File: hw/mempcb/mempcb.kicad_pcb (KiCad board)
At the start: 2 copper layers, 100 x 100 mm, 32 parts, among them J1 RC6502_Bus, J2 0.1" 2x25, U3 JEDEC_DIP32_RAM, U4 74LS138, U5 74LS138

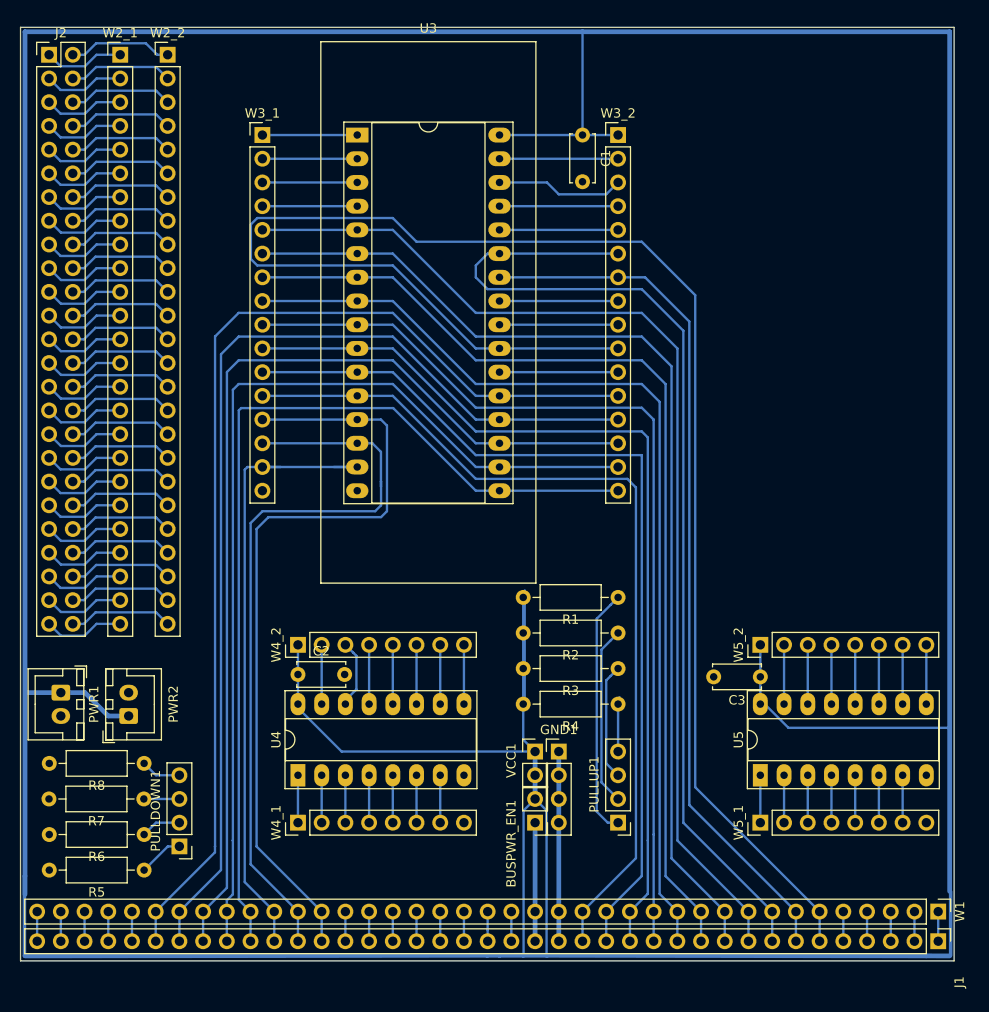
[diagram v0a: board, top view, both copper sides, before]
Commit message: hw/mempcb: Widen board edge to 0.4 mm; tweak corners
According to [1], fabs cut along the _center_ of the board edge line, so
you can make it as wide as you want. Thus a cheap and easy way of ensuring
you maintain margin at the edge of the board is to widen the board line to
twice the margin you need, because KiCad will not let traces etc. _enter_
the line.

I can't check this on 5.0 because the DRC doesn't check for traces
exceeding the board boundary, but I believe that 5.1 does check for this,
so we can test it there.

[1]: https://forum.kicad.info/t/margin-or-edge-cuts/10341/2
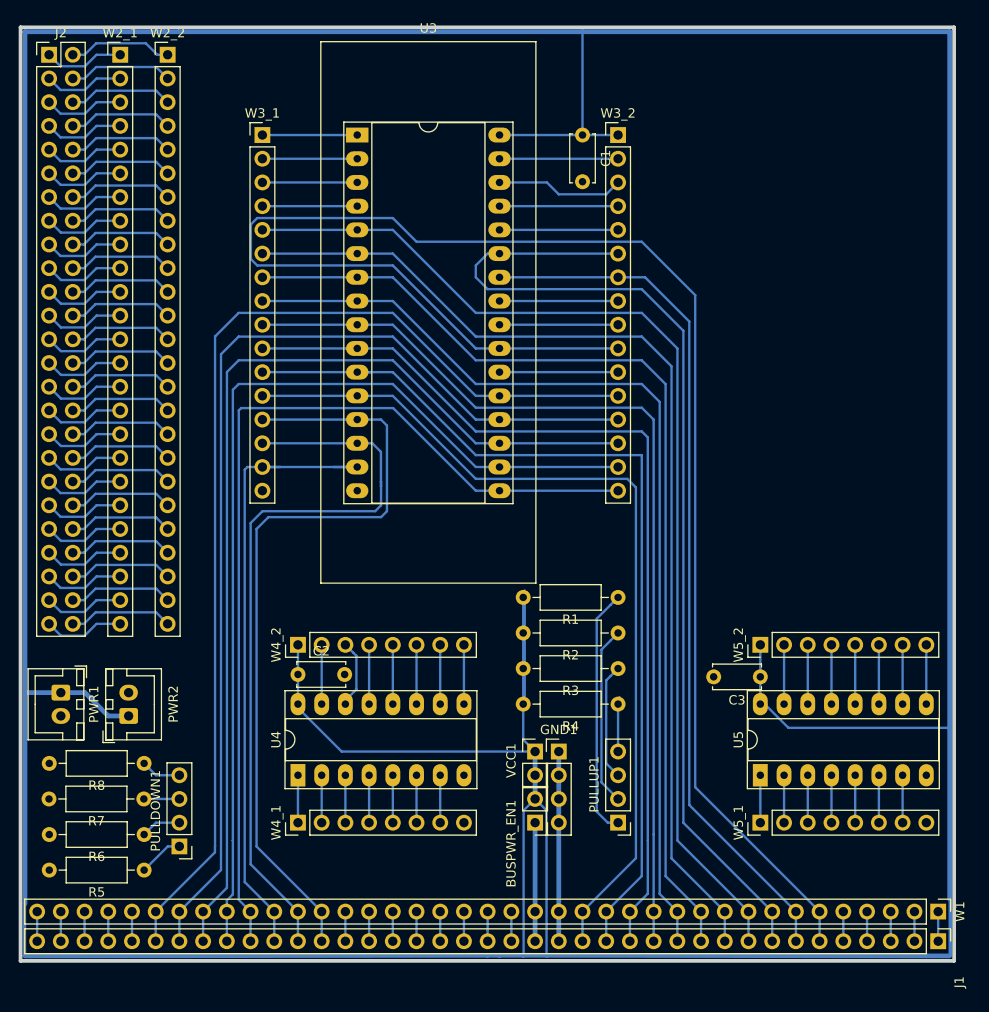
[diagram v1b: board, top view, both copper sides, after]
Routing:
- net /VCC: track 565.0 -> 563.8 mm
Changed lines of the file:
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@@
     (thickness 1.6002)
     (drawings 4)
-    (tracks 525)
+    (tracks 524)
     (zones 0)
     (modules 32)
@@
     )
   )
-  (gr_line (start 101.702 152.102) (end 101.702 52.102) (layer Edge.Cuts) (width 0.0381))
-  (gr_line (start 201.702 152.102) (end 101.702 152.102) (layer Edge.Cuts) (width 0.0381))
-  (gr_line (start 201.702 152.102) (end 201.702 52.102) (layer Edge.Cuts) (width 0.0381))
-  (gr_line (start 101.702 52.102) (end 201.702 52.102) (layer Edge.Cuts) (width 0.0381))
+  (gr_line (start 101.702 152.102) (end 101.702 52.102) (layer Edge.Cuts) (width 0.4))
+  (gr_line (start 201.702 152.102) (end 101.702 152.102) (layer Edge.Cuts) (width 0.4))
+  (gr_line (start 201.702 152.102) (end 201.702 52.102) (layer Edge.Cuts) (width 0.4))
+  (gr_line (start 101.702 52.102) (end 201.702 52.102) (layer Edge.Cuts) (width 0.4))
   (segment (start 153.01 63.64) (end 165.71 63.64) (width 0.254) (layer Back) (net 1) (status 30))
   (segment (start 152.61 63.64) (end 153.01 63.64) (width 0.254) (layer Front) (net 1) (status 30))
@@
   (segment (start 153.01 151.50535) (end 155.56 151.50194) (width 0.508) (layer Back) (net 1))
   (segment (start 201.27 144.693) (end 201.228 144.651) (width 0.254) (layer Back) (net 1))
-  (segment (start 201.334 151.5296) (end 201.334 144.693) (width 0.381) (layer Back) (net 1))
+  (segment (start 201.295 151.5296) (end 201.295 144.693) (width 0.371) (layer Back) (net 1))
   (segment (start 201.228 151.5716) (end 201.27 151.5296) (width 0.254) (layer Back) (net 1))
   (segment (start 198.73 151.567789) (end 201.228 151.5716) (width 0.508) (layer Back) (net 1))
-  (segment (start 102.176 143.015) (end 102.176 145) (width 0.508) (layer Back) (net 1))
-  (segment (start 102.116 151.5716) (end 102.116 143.015) (width 0.381) (layer Back) (net 1))
-  (segment (start 102.176 52.576) (end 102.176 143.015) (width 0.508) (layer Back) (net 1))
+  (segment (start 102.116 151.5716) (end 102.116 146) (width 0.381) (layer Back) (net 1))
+  (segment (start 102.176 52.576) (end 102.176 146) (width 0.508) (layer Back) (net 1))
   (segment (start 161.9 63.64) (end 161.9 52.576) (width 0.254) (layer Back) (net 1))
   (segment (start 161.9 52.576) (end 102.176 52.576) (width 0.508) (layer Back) (net 1))
@@
   (segment (start 201.228 127.14) (end 201.228 52.576) (width 0.508) (layer Back) (net 1))
   (segment (start 183.9598 127.14) (end 201.228 127.14) (width 0.254) (layer Back) (net 1))
-  (segment (start 201.228 144.651) (end 201.228 127.14) (width 0.508) (layer Back) (net 1))
+  (segment (start 201.228 145.5) (end 201.228 127.14) (width 0.508) (layer Back) (net 1))
   (segment (start 131.42 124.6) (end 131.42 118.25) (width 0.254) (layer Back) (net 1))
   (segment (start 151.706 151.50535) (end 153.01 151.50535) (width 0.508) (layer Back) (net 1))

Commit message: hw/mempcb: Clean up board edges and fix clearances
- Move RC6502 bus wire-wrap connector down to be flush against the bus
  bus pins. (The 90 degree connector has a low profile so won't get
  in the way of wire wrap.)
- KiCad 5.1 DRC now checks board edge clearance to center of the edge
  cut line, so we need not check this manually. Thus we can bring board
  edge cut line width back to default 0.0381 to avoid potential problems
  with the fab, and also to have less blocking against edge of cut
  line when routing.
- Redraw the 20 mil outside edge Vcc line now to conform with the default
  0.254 mm clearance (to board edge, in this case).
- Rework the narrower connections on board edge Vcc around the RC6502 bus
  connector to have maximum width possible between the pins and the edge.

TODO:
- Clean up traces at RC6502 bus wire-wrap connector.
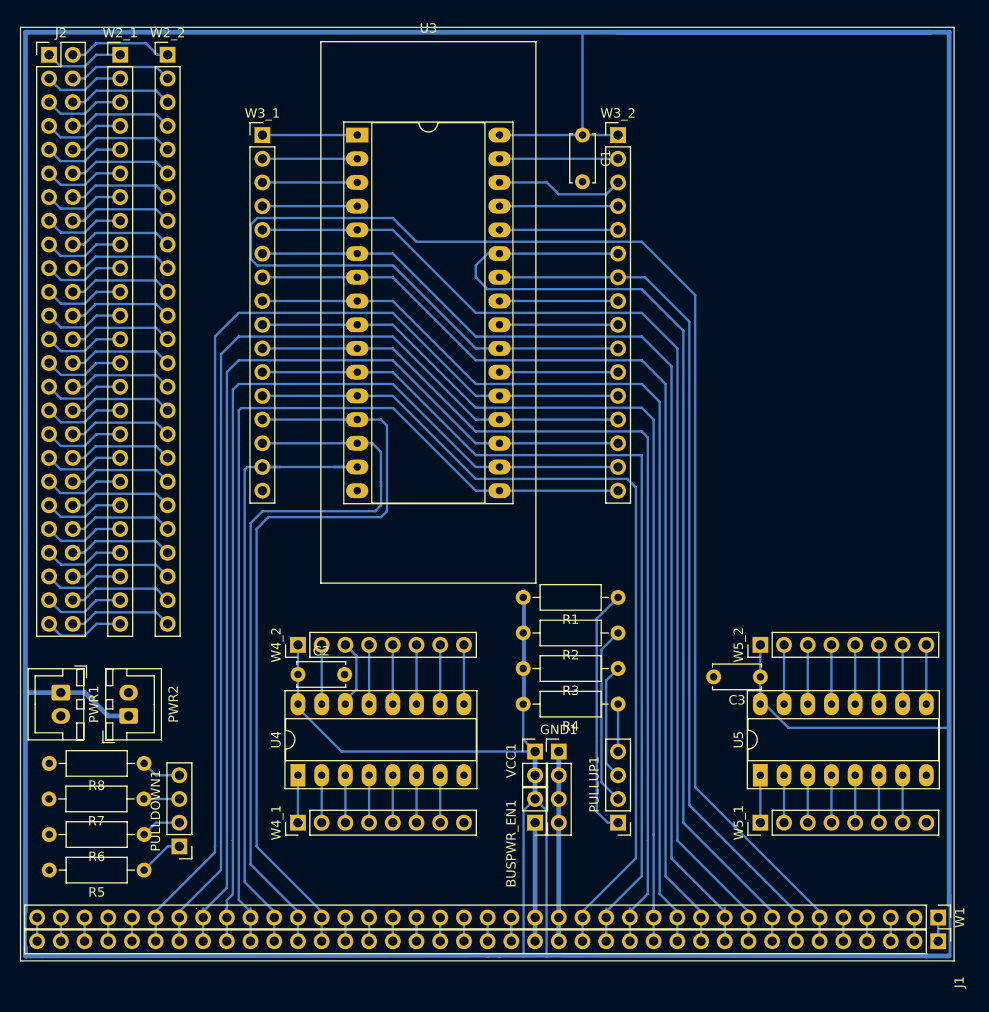
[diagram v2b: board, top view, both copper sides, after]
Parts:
- moved W1 0.64 mm to (200.0, 147.5)
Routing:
- net /VCC: track 563.8 -> 608.6 mm

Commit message: hw/mempcb: Rename most references and remove some from silkscreen
We rename the ICs to U1, U2 and U3 so that it doesn't look like some are
missing. We resolve the previous collisions with the wire-wrap headers by
renaming them all to WW_*.1 and WW_*.2 where * is the part with which
they're associated. The reference alignment and locations are also cleaned
up a bit.

Update the PCB from this, make invisible the skilk screen references for
the WW_* headers (since their associated part is easily clear from
proximity) and for the others move the silk screen to locations that are
more clear.
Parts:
- removed W3_1: 0.1" 1x16, Connector_PinHeader_2.54mm:PinHeader_1x16_P2.54mm_Vertical
- added WW_U1.1: 0.1" 1x16, Connector_PinHeader_2.54mm:PinHeader_1x16_P2.54mm_Vertical, F.Cu at (127.6, 63.6)
- renumbered U3 to U1, U4 to U2, U5 to U3, W1 to WW_J1, W2_1 to WW_J2.1, W2_2 to WW_J2.2, W3_2 to WW_U1.2, W4_1 to WW_U2.1, W4_2 to WW_U2.2, W5_1 to WW_U3.1, W5_2 to WW_U3.2

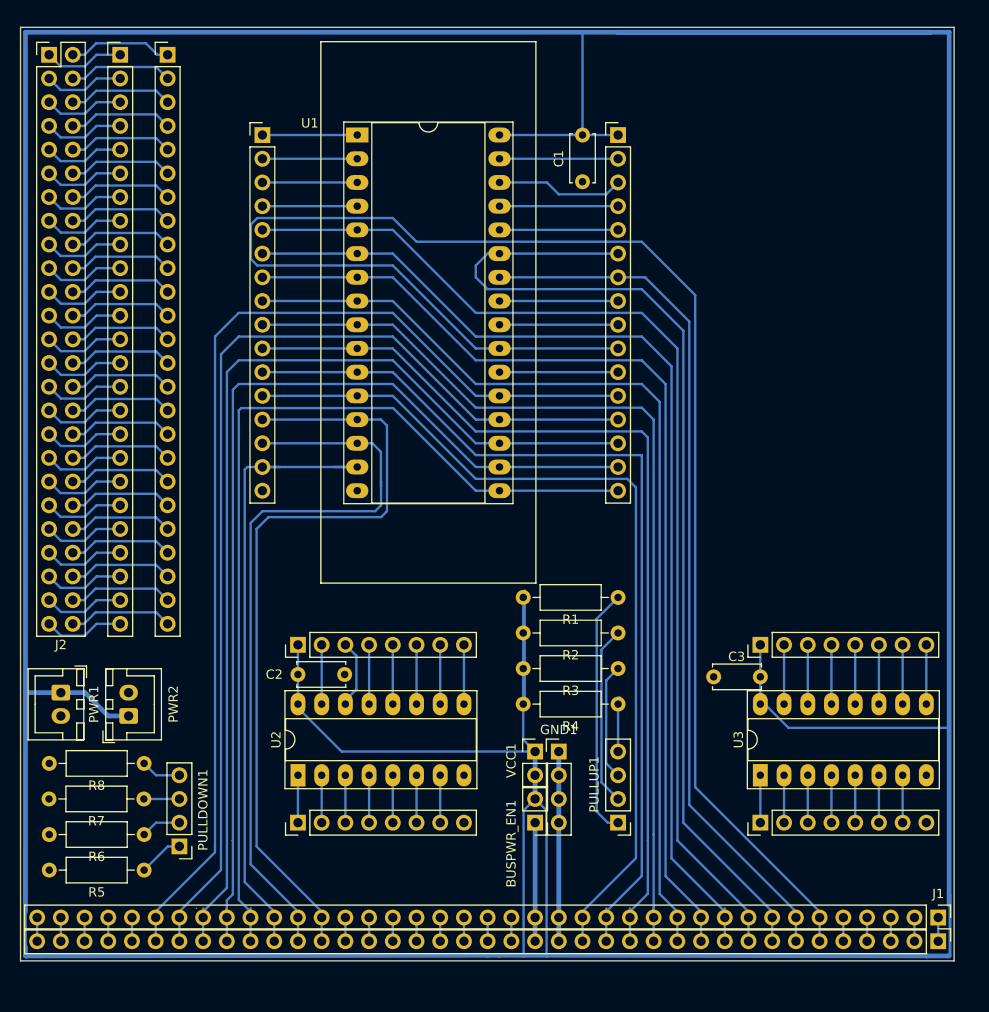
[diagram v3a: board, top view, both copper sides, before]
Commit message: hw/mempcb: Rename, rework and swap position of pull-ups/downs
- Rename PULLDOWN1 to PULLDOWN2
- Rename associated resistors to R1.1, R1.2 etc. for PULLUP1, and R2.1,
  R2.2 for PULLDOWN2.
- Make the resistor silks smaller, rotated and across the middle, so that
  they're out of the way but readable under the resistor, now now one can
  see which pins on the header they match. Nonetheless, also add pin
  numbers to the PULLDOWN2 header, since it's not lined up with the
  resistors like PULLUP1 is.
- Swap the pull-ups and pull-downs: having the pull-ups next to the power
  connectors is a bit more intuitive, and also makes for easier power
  distribution.

Also remove a couple of unconnected traces on the RC6502 header.
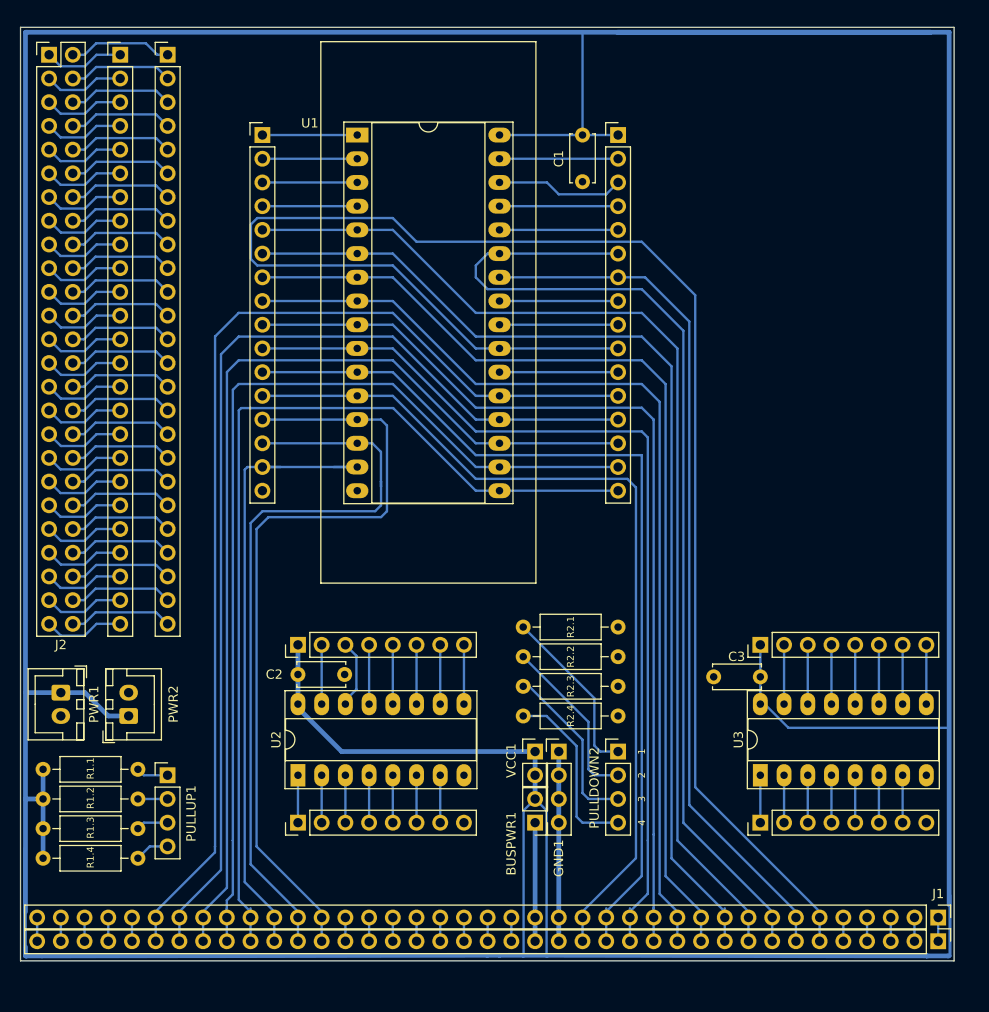
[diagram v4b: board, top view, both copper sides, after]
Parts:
- removed PULLDOWN1: 0.1" 1x4, Connector_PinHeader_2.54mm:PinHeader_1x04_P2.54mm_Vertical
- added PULLDOWN2: 0.1" 1x4, Connector_PinHeader_2.54mm:PinHeader_1x04_P2.54mm_Vertical, F.Cu at (165.7, 129.7)
- moved R1.1 54.6 mm to (114.3, 131.6)
- moved R1.2 54.4 mm to (114.3, 134.8)
- moved R1.3 54.2 mm to (114.3, 137.9)
- moved R1.4 54.0 mm to (114.3, 141.1)
- moved PULLUP1 48.5 mm to (117.5, 132.2), turned to 0 degrees
- moved R2.1 48.2 mm to (155.6, 116.3), turned to 0 degrees
- moved R2.2 44.9 mm to (155.6, 119.5), turned to 0 degrees
- moved R2.3 42.4 mm to (155.6, 122.7), turned to 0 degrees
- moved R2.4 40.9 mm to (155.6, 125.9), turned to 0 degrees
- renumbered BUSPWR_EN1 to BUSPWR1, R1 to R1.1, R2 to R1.2, R3 to R1.3, R4 to R1.4, R5 to R2.1, R6 to R2.2, R7 to R2.3, R8 to R2.4
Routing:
- net Net-(PULLUP1-Pad1): track 26.7 -> 4.34 mm
- net /VCC: track 608.6 -> 591.5 mm
- net Net-(PULLUP1-Pad2): track 19.3 -> 3.17 mm
- net Net-(PULLDOWN2-Pad4): track 4.31 -> 19.3 mm
- net Net-(PULLDOWN2-Pad3): track 3.81 -> 18.5 mm
- net Net-(PULLDOWN2-Pad2): track 4.31 -> 18.4 mm
- net Net-(PULLDOWN2-Pad1): track 4.83 -> 18.7 mm
- net Net-(PULLUP1-Pad3): track 12.5 -> 3.44 mm
- net Net-(PULLUP1-Pad4): track 5.29 -> 3.70 mm

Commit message: hw/mempcb: Clean up addr/data lines at RC6502 header
This fixes the weird pad entries that were left after moving
the wire-wrap header down to butt against the bus connector.
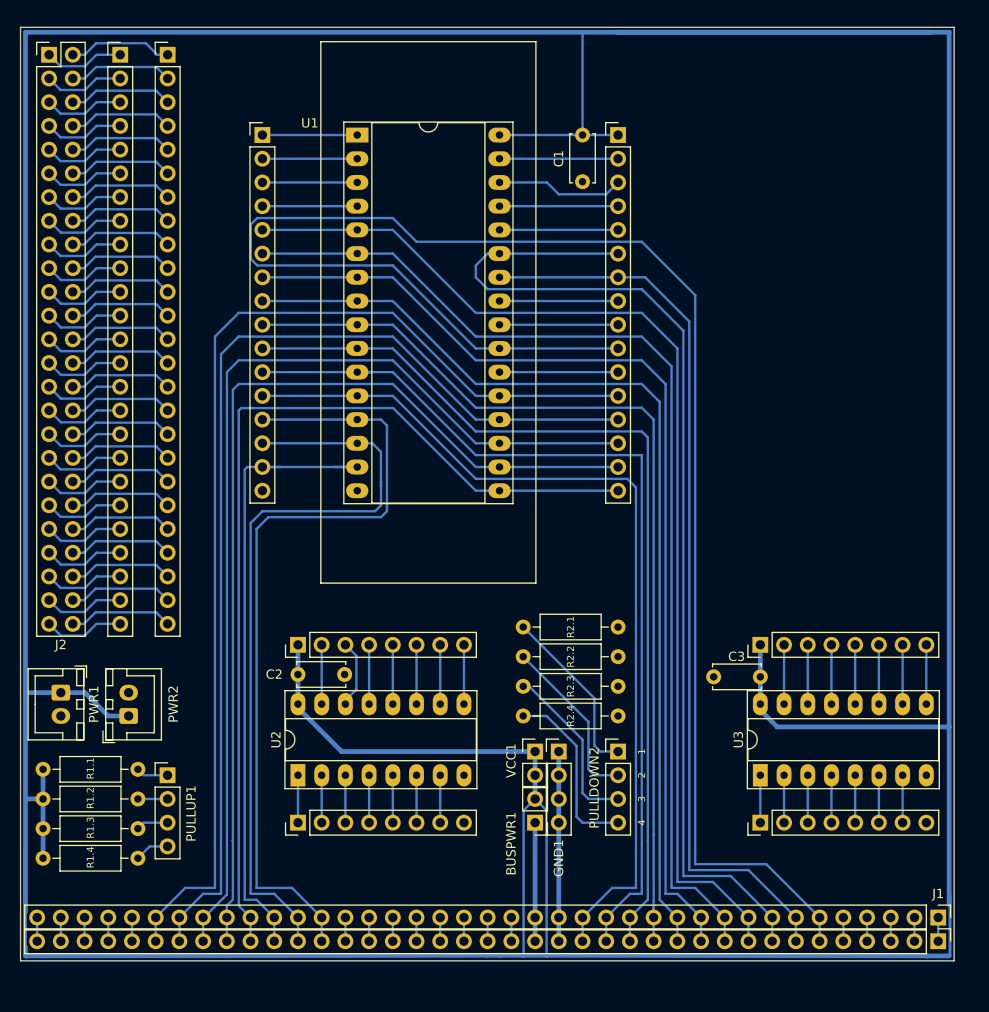
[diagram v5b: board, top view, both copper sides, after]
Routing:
- net /A10: track 173.4 -> 177.9 mm
- net /A9: track 93.4 -> 97.1 mm
- net /A8: track 111.0 -> 113.9 mm
- net /D0: track 84.9 -> 87.7 mm
- net /A7: track 116.4 -> 118.6 mm
- net /D7: track 115.3 -> 117.2 mm
- net /A0: track 95.1 -> 96.5 mm
- net /D1: track 81.0 -> 82.5 mm
- net /A6: track 113.1 -> 114.3 mm
- net /D6: track 111.7 -> 112.8 mm
- net /A5: track 109.2 -> 109.9 mm
- net /D2: track 68.4 -> 69.2 mm
- net /VCC: track 591.5 -> 592.1 mm
